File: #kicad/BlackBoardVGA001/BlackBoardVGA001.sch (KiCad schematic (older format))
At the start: 25 parts, among them J1 VGA, J2 PS/2, J3 Left, J4 Right, J5 LAN8720

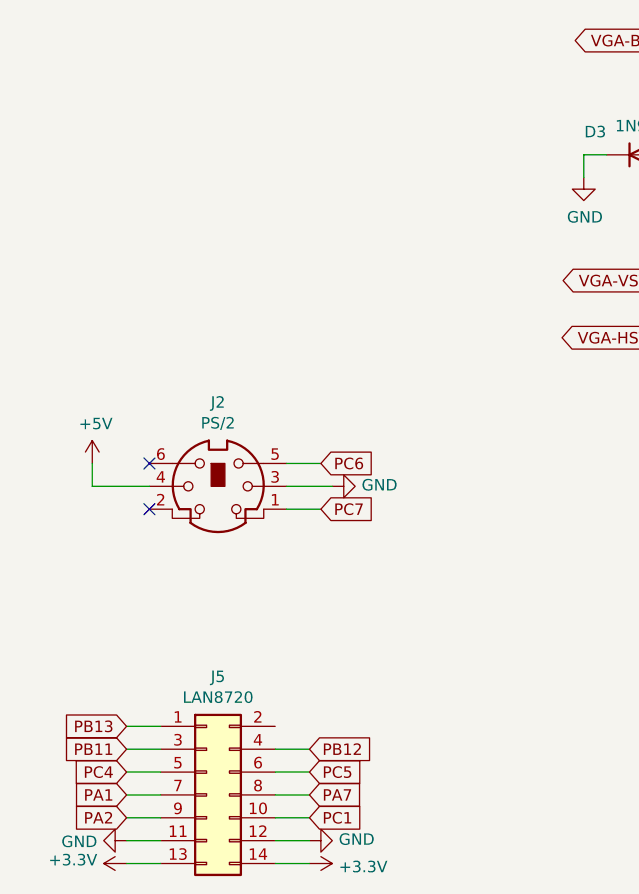
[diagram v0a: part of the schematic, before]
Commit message: added a second ps2 connector, eventually for mouse (not connected to any gpio yet)
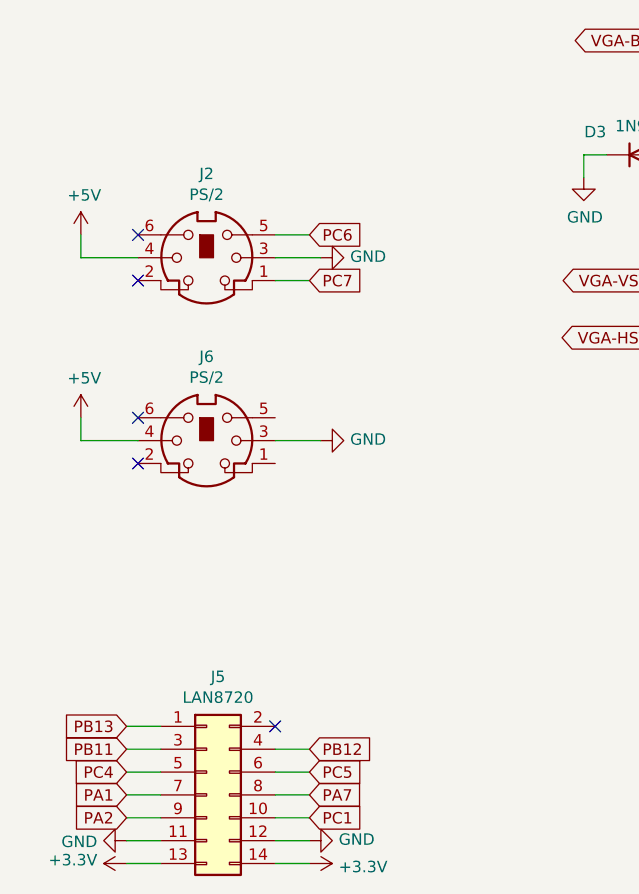
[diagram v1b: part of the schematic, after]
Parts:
- added J6: PS/2, BlackBoardVGA001:Mini_din6, symbol Connector:Mini-DIN-6
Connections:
- net +5V: now also J6.4
- net GND: now also J6.3
- no-connect marks 7 -> 10
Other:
- moved on the sheet: J2
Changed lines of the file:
@@
 L Connector:Mini-DIN-6 J2
 U 1 1 5EE80465
-P 1750 4950
-F 0 "J2" H 1750 5317 50  0000 C CNN
-F 1 "PS/2" H 1750 5226 50  0000 C CNN
-F 2 "BlackBoardVGA001:Mini_din6" H 1750 4950 50  0001 C CNN
-F 3 "http://service.powerdynamics.com/ec/Catalog17/Section%2011.pdf" H 1750 4950 50  0001 C CNN
-	1    1750 4950
+P 1700 3950
+F 0 "J2" H 1700 4317 50  0000 C CNN
+F 1 "PS/2" H 1700 4226 50  0000 C CNN
+F 2 "BlackBoardVGA001:Mini_din6" H 1700 3950 50  0001 C CNN
+F 3 "http://service.powerdynamics.com/ec/Catalog17/Section%2011.pdf" H 1700 3950 50  0001 C CNN
+	1    1700 3950
 	1    0    0    -1
 $EndComp
@@
 L power:GND #PWR03
 U 1 1 5F261B1F
-P 2250 4950
-F 0 "#PWR03" H 2250 4700 50  0001 C CNN
-F 1 "GND" V 2255 4822 50  0000 R CNN
-F 2 "" H 2250 4950 50  0001 C CNN
-F 3 "" H 2250 4950 50  0001 C CNN
-	1    2250 4950
+P 2200 3950
+F 0 "#PWR03" H 2200 3700 50  0001 C CNN
+F 1 "GND" V 2205 3822 50  0000 R CNN
+F 2 "" H 2200 3950 50  0001 C CNN
+F 3 "" H 2200 3950 50  0001 C CNN
+	1    2200 3950
 	0    -1   -1   0
 $EndComp
@@
 L power:+5V #PWR02
 U 1 1 5F262726
-P 1200 4850
-F 0 "#PWR02" H 1200 4700 50  0001 C CNN
-F 1 "+5V" H 1215 5023 50  0000 C CNN
-F 2 "" H 1200 4850 50  0001 C CNN
-F 3 "" H 1200 4850 50  0001 C CNN
-	1    1200 4850
-	1    0    0    -1
-$EndComp
-Wire Wire Line
-	2050 4950 2250 4950
-Wire Wire Line
-	1450 4950 1200 4950
-Wire Wire Line
-	1200 4950 1200 4850
+P 1150 3850
+F 0 "#PWR02" H 1150 3700 50  0001 C CNN
+F 1 "+5V" H 1165 4023 50  0000 C CNN
+F 2 "" H 1150 3850 50  0001 C CNN
+F 3 "" H 1150 3850 50  0001 C CNN
+	1    1150 3850
+	1    0    0    -1
+$EndComp
+Wire Wire Line
+	2000 3950 2200 3950
+Wire Wire Line
+	1400 3950 1150 3950
+Wire Wire Line
+	1150 3950 1150 3850
 $Comp
 L Diode:1N914 D2
@@
 NoConn ~ 1700 1300
 NoConn ~ 2300 1100
-NoConn ~ 1450 4850
-NoConn ~ 1450 5050
+NoConn ~ 1400 3850
+NoConn ~ 1400 4050
 $Comp
 L power:GND #PWR017
@@
 Wire Wire Line
 	2000 2300 2000 2400
-Text GLabel 2200 4850 2    50   Input ~ 0
+Text GLabel 2150 3850 2    50   Input ~ 0
 PC6
-Text GLabel 2200 5050 2    50   Input ~ 0
+Text GLabel 2150 4050 2    50   Input ~ 0
 PC7
 Wire Wire Line
-	2050 4850 2200 4850
-Wire Wire Line
-	2050 5050 2200 5050
+	2000 3850 2150 3850
+Wire Wire Line
+	2000 4050 2150 4050
 $Comp
 L Connector_Generic:Conn_02x07_Odd_Even J5
@@
 Wire Wire Line
 	4400 3500 4850 3500
+$Comp
+L Connector:Mini-DIN-6 J6
+U 1 1 5F04A1FF
+P 1700 4750
+F 0 "J6" H 1700 5117 50  0000 C CNN
+F 1 "PS/2" H 1700 5026 50  0000 C CNN
+F 2 "BlackBoardVGA001:Mini_din6" H 1700 4750 50  0001 C CNN
+F 3 "http://service.powerdynamics.com/ec/Catalog17/Section%2011.pdf" H 1700 4750 50  0001 C CNN
+	1    1700 4750
+	1    0    0    -1
+$EndComp
+$Comp
+L power:GND #PWR024
+U 1 1 5F04B660
+P 2200 4750
+F 0 "#PWR024" H 2200 4500 50  0001 C CNN
+F 1 "GND" V 2205 4622 50  0000 R CNN
+F 2 "" H 2200 4750 50  0001 C CNN
+F 3 "" H 2200 4750 50  0001 C CNN
+	1    2200 4750
+	0    -1   -1   0
+$EndComp
+$Comp
+L power:+5V #PWR023
+U 1 1 5F04BB87
+P 1150 4650
+F 0 "#PWR023" H 1150 4500 50  0001 C CNN
+F 1 "+5V" H 1165 4823 50  0000 C CNN
+F 2 "" H 1150 4650 50  0001 C CNN
+F 3 "" H 1150 4650 50  0001 C CNN
+	1    1150 4650
+	1    0    0    -1
+$EndComp
+Wire Wire Line
+	2000 4750 2200 4750
+Wire Wire Line
+	1150 4650 1150 4750
+Wire Wire Line
+	1150 4750 1400 4750
+NoConn ~ 1400 4650
+NoConn ~ 1400 4850
+NoConn ~ 2000 6000
 $EndSCHEMATC

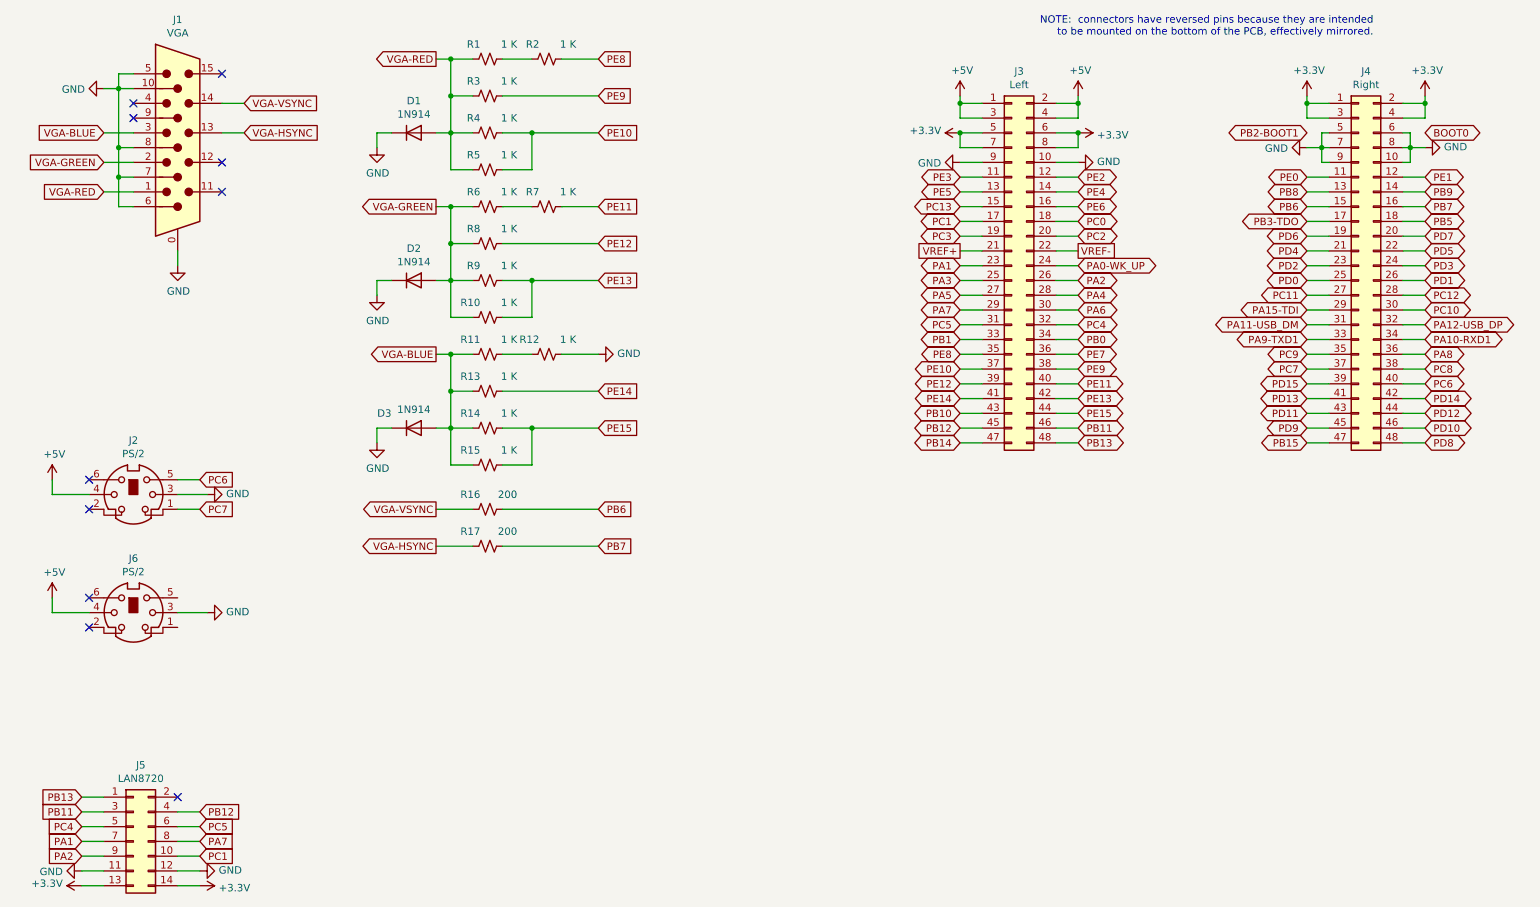
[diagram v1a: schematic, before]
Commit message: using E0 and E1 for second PS/2
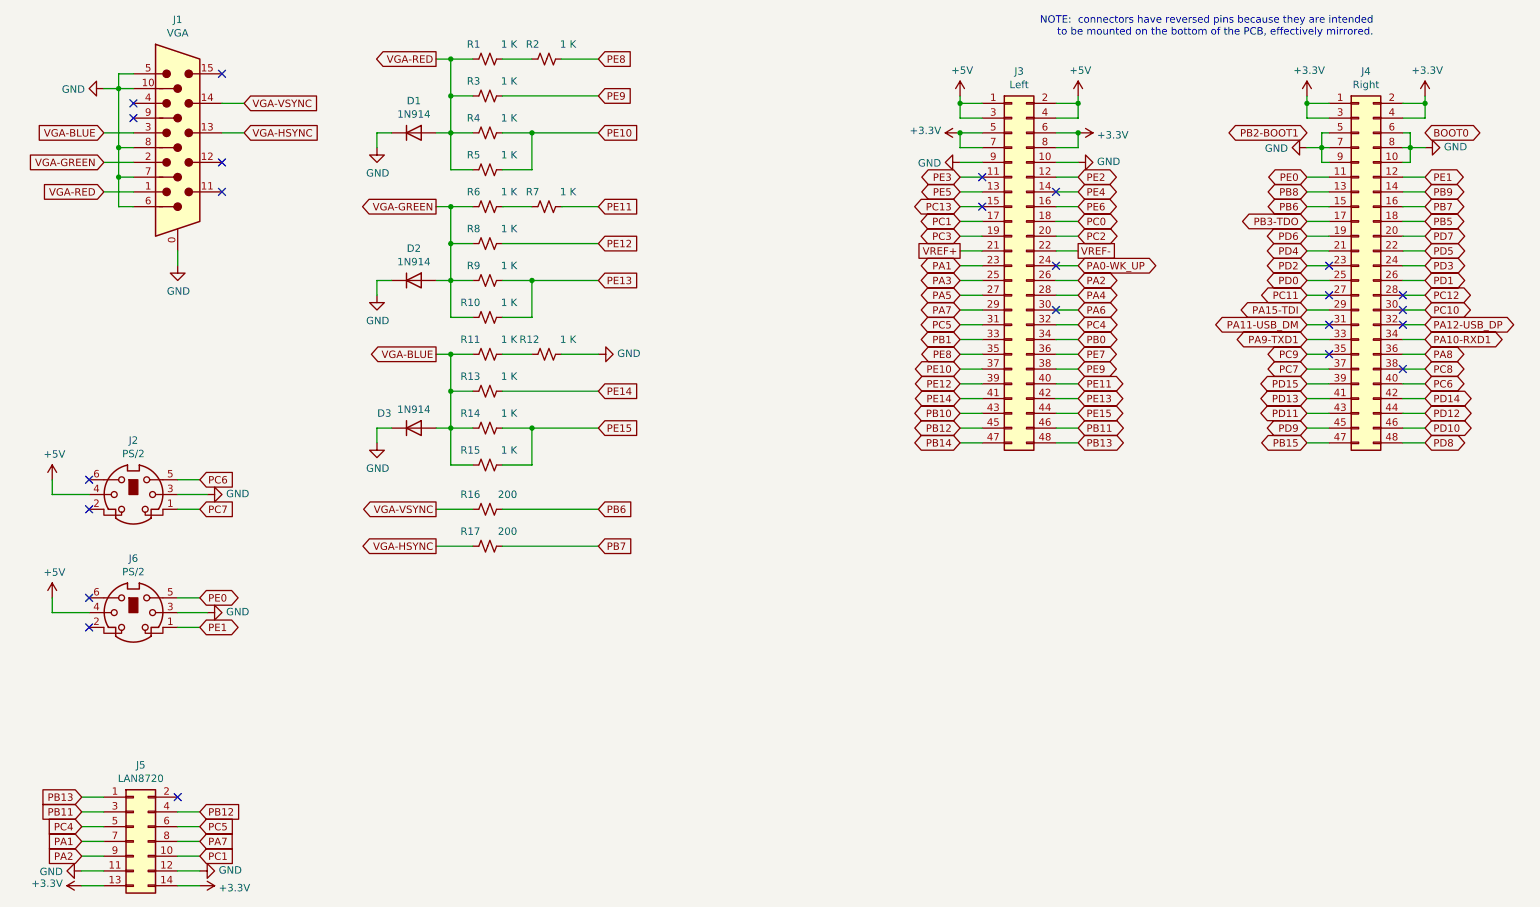
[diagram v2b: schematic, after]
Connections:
- net PE0: now also J6.5
- net PE1: now also J6.1
- no-connect marks 10 -> 23
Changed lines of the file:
@@
 Text GLabel 10450 3100 2    50   BiDi ~ 0
 PC8
-Text GLabel 10450 3200 2    50   BiDi ~ 0
-PC6
 Text GLabel 10450 3300 2    50   BiDi ~ 0
 PD14
@@
 NoConn ~ 1400 4850
 NoConn ~ 2000 6000
+Text GLabel 10450 3200 2    50   BiDi ~ 0
+PC6
+NoConn ~ 10300 3100
+NoConn ~ 9800 3000
+NoConn ~ 9800 2800
+NoConn ~ 10300 2800
+NoConn ~ 10300 2700
+NoConn ~ 10300 2600
+NoConn ~ 9800 2600
+NoConn ~ 9800 2400
+NoConn ~ 7450 1800
+NoConn ~ 7950 1900
+NoConn ~ 7450 2000
+NoConn ~ 7950 2700
+NoConn ~ 7950 2400
+Text GLabel 2150 4650 2    50   BiDi ~ 0
+PE0
+Text GLabel 2150 4850 2    50   BiDi ~ 0
+PE1
+Wire Wire Line
+	2000 4650 2150 4650
+Wire Wire Line
+	2000 4850 2150 4850
 $EndSCHEMATC
